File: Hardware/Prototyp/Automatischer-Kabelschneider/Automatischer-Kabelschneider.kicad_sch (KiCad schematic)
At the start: 0 parts

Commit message: 20240411
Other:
- sheet Powersupply_AKS ports: added D+, D-; removed none
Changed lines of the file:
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@@
+			)
+		)
+		(pin "D+" input
+			(at 149.86 62.23 0)
+			(effects
+				(font
+					(size 1.27 1.27)
+				)
+				(justify right)
+			)
+		)
+		(pin "D-" input
+			(at 149.86 64.77 0)
+			(effects
+				(font
+					(size 1.27 1.27)
+				)
+				(justify right)
 			)
 		)

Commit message: 20240415
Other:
- sheet Main Microcontroller ports: added D+, D-; removed none
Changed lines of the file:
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@@
 		(comment 1 "This is the main schematic sheet of this KiCad Project")
+	)
+	(wire
+		(pts
+			(xy 158.75 90.17) (xy 158.75 62.23)
+		)
+		(stroke
+			(width 0)
+			(type default)
+		)
+	)
+	(wire
+		(pts
+			(xy 140.97 86.36) (xy 153.67 86.36)
+		)
+		(stroke
+			(width 0)
+			(type default)
+		)
+	)
+	(wire
+		(pts
+			(xy 158.75 62.23) (xy 149.86 62.23)
+		)
+		(stroke
+			(width 0)
+			(type default)
+		)
+	)
+	(wire
+		(pts
+			(xy 140.97 90.17) (xy 158.75 90.17)
+		)
+		(stroke
+			(width 0)
+			(type default)
+		)
+	)
+	(wire
+		(pts
+			(xy 153.67 64.77) (xy 149.86 64.77)
+		)
+		(stroke
+			(width 0)
+			(type default)
+		)
+	)
+	(wire
+		(pts
+			(xy 153.67 86.36) (xy 153.67 64.77)
+		)
+		(stroke
+			(width 0)
+			(type default)
+		)
 	)
 	(sheet
@@
 				)
 				(justify left top)
+			)
+		)
+		(pin "D-" bidirectional
+			(at 140.97 86.36 0)
+			(effects
+				(font
+					(size 1.27 1.27)
+				)
+				(justify right)
+			)
+		)
+		(pin "D+" bidirectional
+			(at 140.97 90.17 0)
+			(effects
+				(font
+					(size 1.27 1.27)
+				)
+				(justify right)
 			)
 		)
@@
 			)
 		)
-		(pin "D+" input
+		(pin "D+" bidirectional
 			(at 149.86 62.23 0)
 			(effects
@@
 			)
 		)
-		(pin "D-" input
+		(pin "D-" bidirectional
 			(at 149.86 64.77 0)
 			(effects

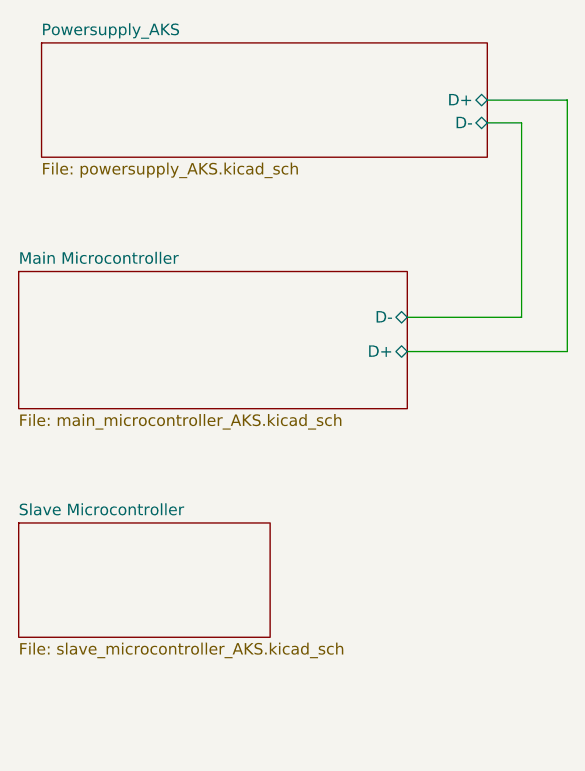
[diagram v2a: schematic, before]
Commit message: Schematic completed
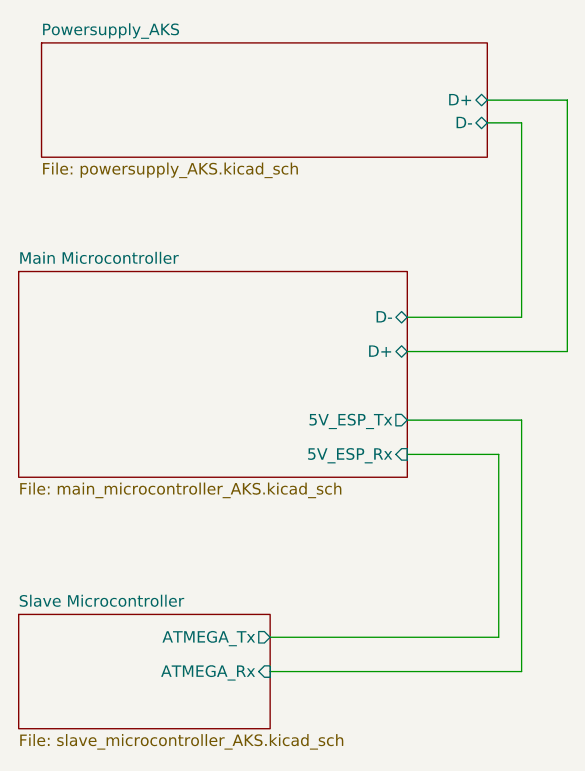
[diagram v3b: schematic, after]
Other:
- sheet Main Microcontroller ports: added 5V_ESP_Rx, 5V_ESP_Tx; removed none
- sheet Slave Microcontroller ports: added ATMEGA_Rx, ATMEGA_Tx; removed none
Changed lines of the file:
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@@
+	(wire
+		(pts
+			(xy 153.67 125.73) (xy 153.67 97.79)
+		)
+		(stroke
+			(width 0)
+			(type default)
+		)
+	)
+	(wire
+		(pts
+			(xy 153.67 97.79) (xy 140.97 97.79)
+		)
+		(stroke
+			(width 0)
+			(type default)
+		)
+	)
+	(wire
+		(pts
+			(xy 125.73 121.92) (xy 151.13 121.92)
+		)
+		(stroke
+			(width 0)
+			(type default)
+		)
+	)
 	(wire
 		(pts
@@
 	(wire
 		(pts
+			(xy 151.13 101.6) (xy 140.97 101.6)
+		)
+		(stroke
+			(width 0)
+			(type default)
+		)
+	)
+	(wire
+		(pts
 			(xy 140.97 90.17) (xy 158.75 90.17)
 		)
@@
 	(wire
 		(pts
+			(xy 151.13 121.92) (xy 151.13 101.6)
+		)
+		(stroke
+			(width 0)
+			(type default)
+		)
+	)
+	(wire
+		(pts
 			(xy 153.67 86.36) (xy 153.67 64.77)
+		)
+		(stroke
+			(width 0)
+			(type default)
+		)
+	)
+	(wire
+		(pts
+			(xy 125.73 125.73) (xy 153.67 125.73)
 		)
 		(stroke
@@
 	(sheet
 		(at 97.79 81.28)
-		(size 43.18 15.24)
+		(size 43.18 22.86)
 		(fields_autoplaced yes)
 		(stroke
@@
 		)
 		(property "Sheetfile" "main_microcontroller_AKS.kicad_sch"
-			(at 97.79 97.1046 0)
+			(at 97.79 104.7246 0)
 			(effects
 				(font
@@
 		(pin "D+" bidirectional
 			(at 140.97 90.17 0)
+			(effects
+				(font
+					(size 1.27 1.27)
+				)
+				(justify right)
+			)
+		)
+		(pin "5V_ESP_Rx" input
+			(at 140.97 101.6 0)
+			(effects
+				(font
+					(size 1.27 1.27)
+				)
+				(justify right)
+			)
+		)
+		(pin "5V_ESP_Tx" output
+			(at 140.97 97.79 0)
 			(effects
 				(font
@@
 	)
 	(sheet
-		(at 97.79 109.22)
+		(at 97.79 119.38)
 		(size 27.94 12.7)
 		(fields_autoplaced yes)
@@
 		)
 		(property "Sheetname" "Slave Microcontroller"
-			(at 97.79 108.5084 0)
+			(at 97.79 118.6684 0)
 			(effects
 				(font
@@
 		)
 		(property "Sheetfile" "slave_microcontroller_AKS.kicad_sch"
-			(at 97.79 122.5046 0)
+			(at 97.79 132.6646 0)
 			(effects
 				(font
@@
 			)
 		)
+		(pin "ATMEGA_Tx" output
+			(at 125.73 121.92 0)
+			(effects
+				(font
+					(size 1.27 1.27)
+				)
+				(justify right)
+			)
+		)
+		(pin "ATMEGA_Rx" input
+			(at 125.73 125.73 0)
+			(effects
+				(font
+					(size 1.27 1.27)
+				)
+				(justify right)
+			)
+		)
